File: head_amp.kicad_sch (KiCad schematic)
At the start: 50 parts, among them J1 USB Port, J2 I2C, J3 LED, J4 Left_Mic, J5 Left_Speaker, J6 Right_Mic, J7 Right_Speaker, J8 Fan, Q1 MMBT3904, Q2 MMBT3904, Q3 AO3401A, Q4 AO3400A, SW1 SW_Push, SW2 SW_Push, U1 AMS1117-3.3, U2 CH340K, U4 Headphone Jack, U7 AMS1117-3.3, U8 ESP32-WROOM-32E

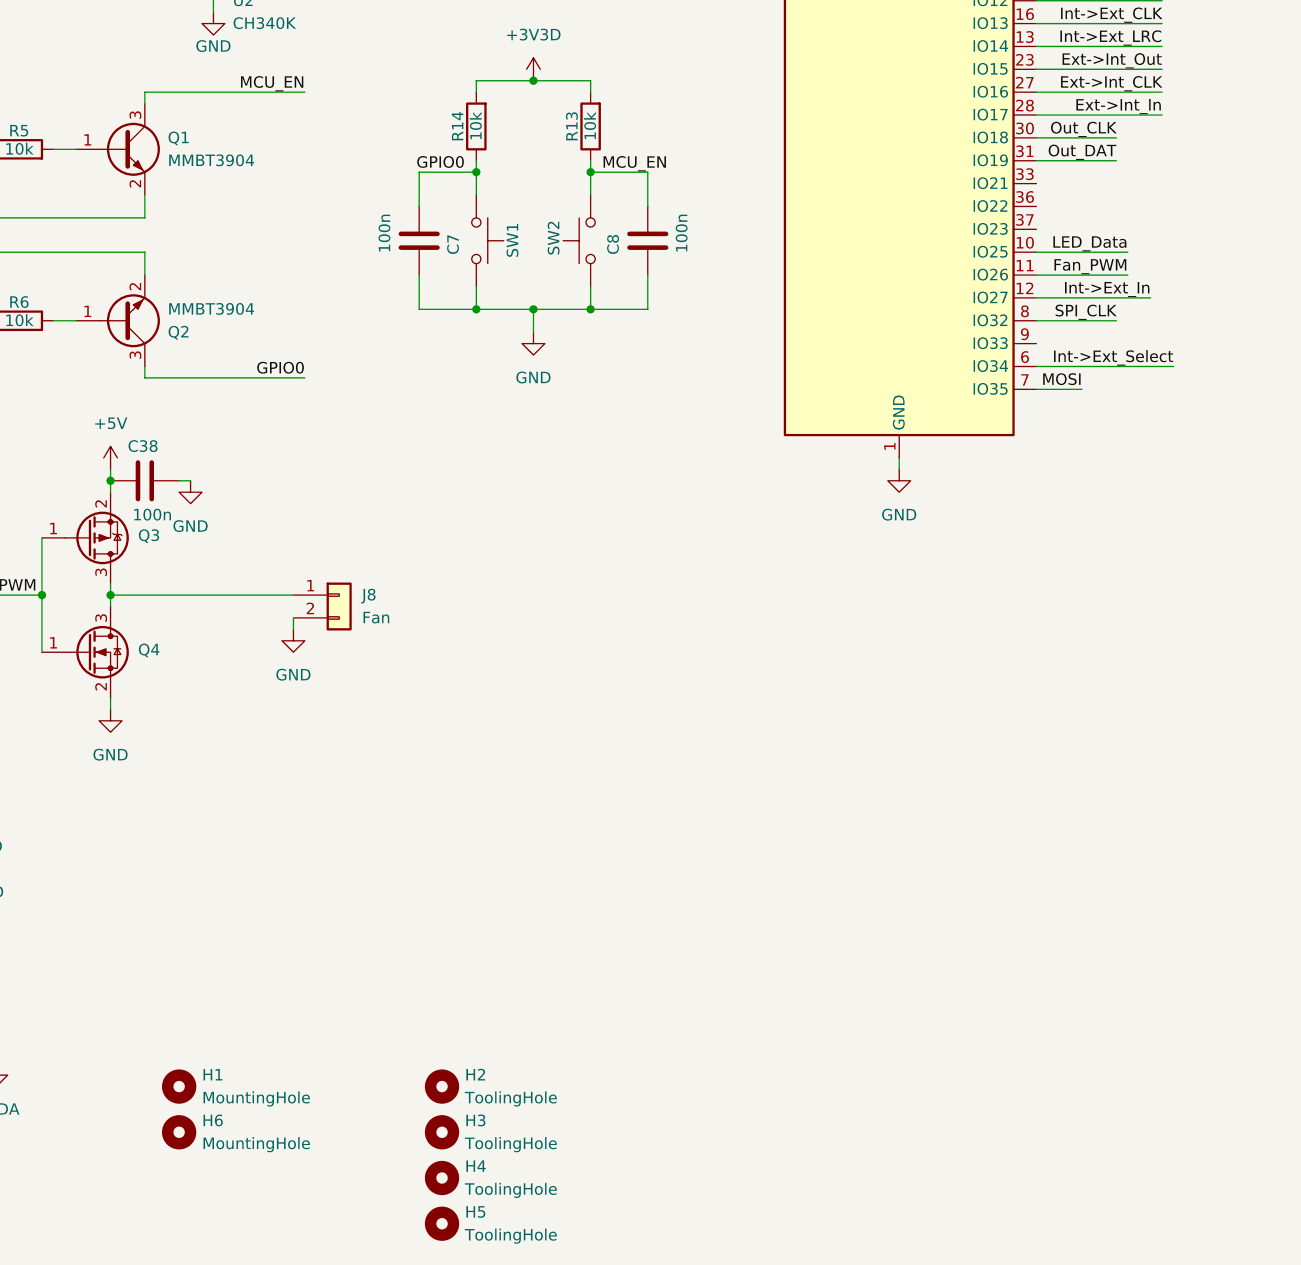
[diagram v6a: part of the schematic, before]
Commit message: Add holes and generic control button
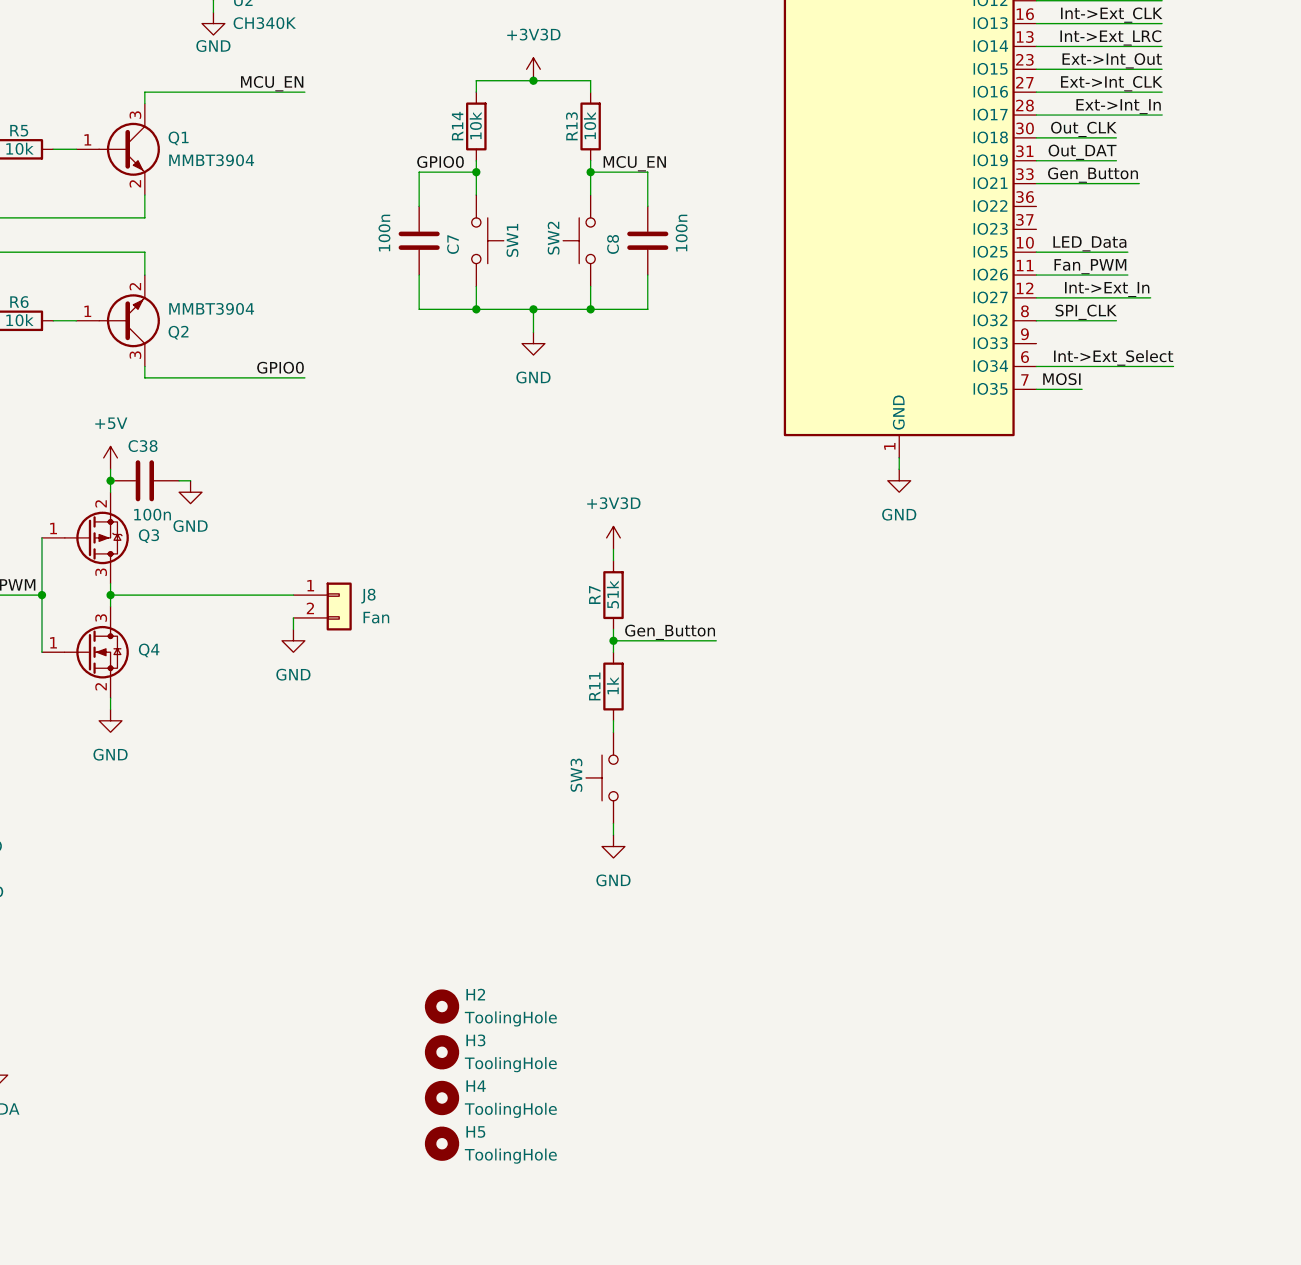
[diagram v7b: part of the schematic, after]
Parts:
- removed H1, H6: MountingHole, MountingHole:MountingHole_3.2mm_M3, symbol Mechanical:MountingHole
- added R11: 1k, Resistor_SMD:R_0402_1005Metric, symbol Device:R
- added R7: 51k, Resistor_SMD:R_0402_1005Metric, symbol Device:R
- added SW3: SW_Push, Button_Switch_SMD:SW_SPST_TS-1088-xR020, symbol Switch:SW_Push
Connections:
- net +3V3D: now also R7.2
- net GND: now also SW3.1
- net Gen_Button: now reaches U8.33 (IO21)
- net Gen_Button: now also R11.2, R7.1
- new net: R11.1, SW3.2
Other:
- moved on the sheet: H2, H3, H4, H5

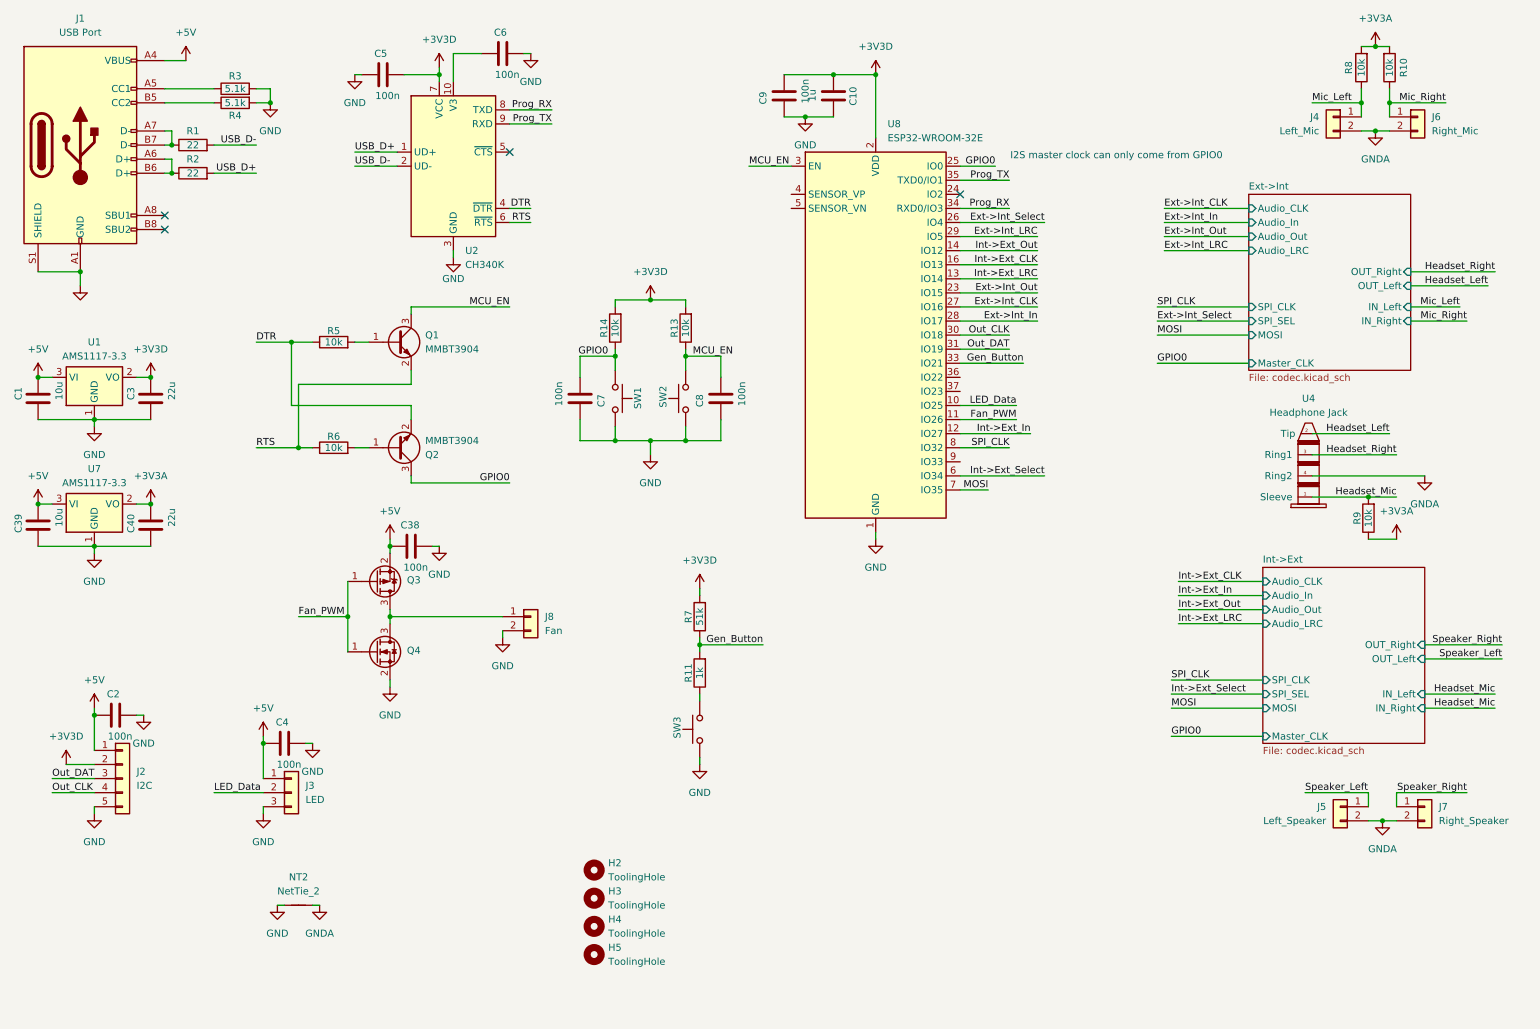
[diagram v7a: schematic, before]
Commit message: Add second expansion port
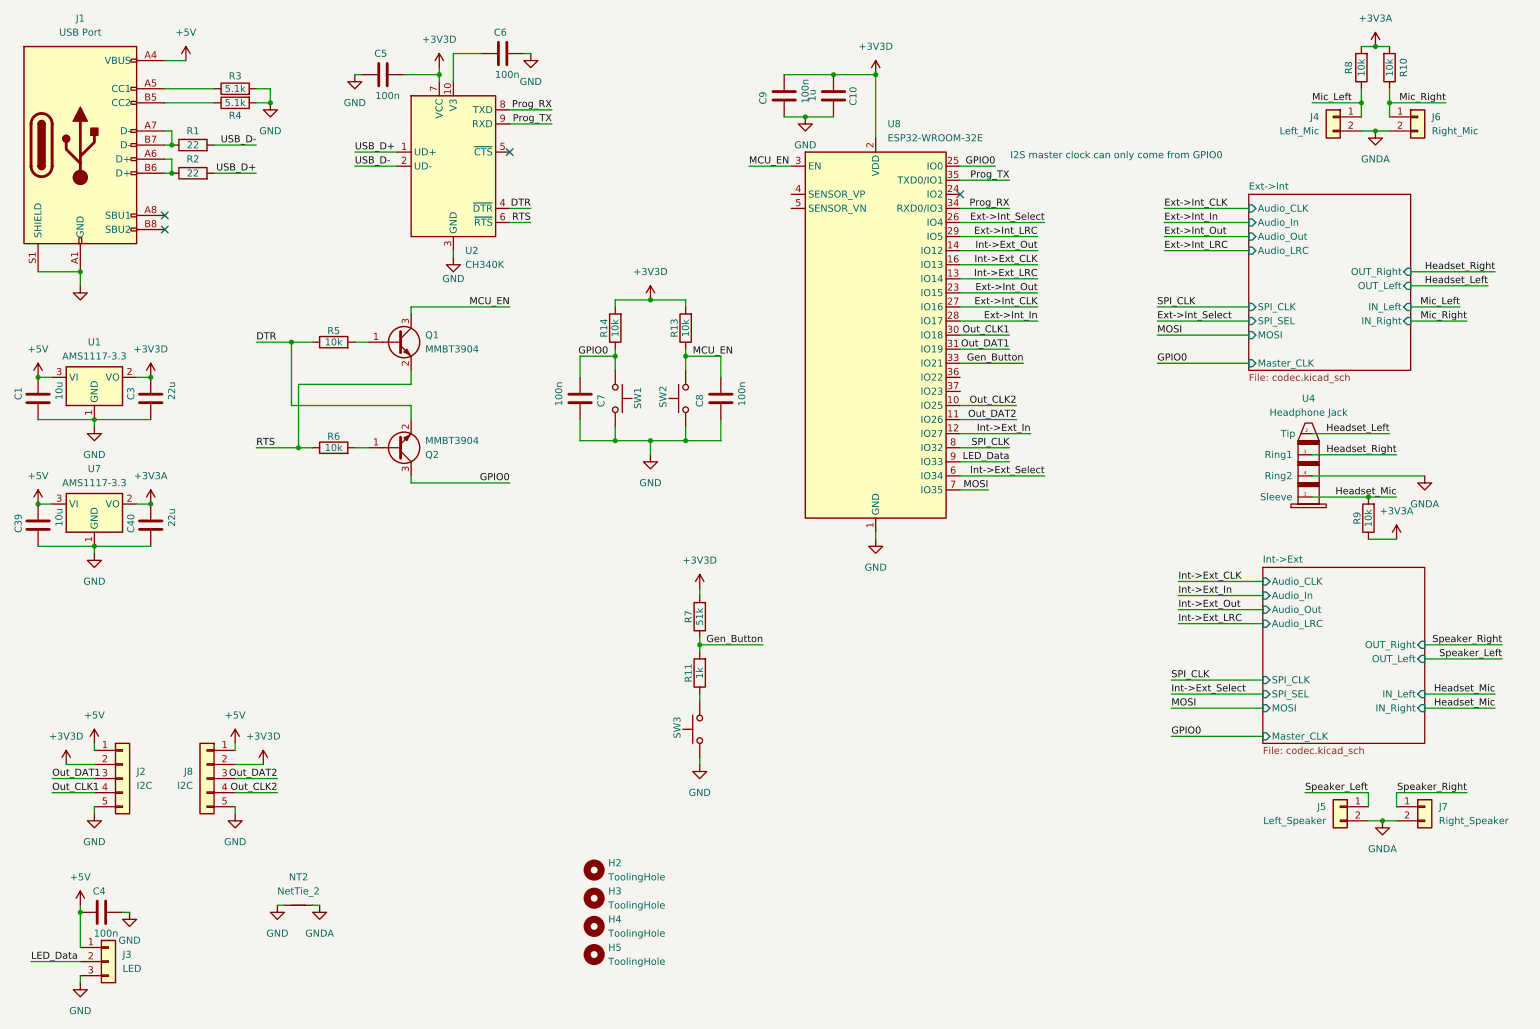
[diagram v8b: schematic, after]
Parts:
- removed C2, C38: 100n, Capacitor_SMD:C_0603_1608Metric, symbol Device:C
- removed J8: Fan, Connector_JST:JST_EH_S2B-EH_1x02_P2.50mm_Horizontal, symbol Connector_Generic:Conn_01x02
- removed Q3: AO3401A, Package_TO_SOT_SMD:SOT-23, symbol Transistor_FET:AO3401A
- removed Q4: AO3400A, Package_TO_SOT_SMD:SOT-23, symbol Transistor_FET:AO3400A
- added J8: I2C, Connector_JST:JST_EH_S5B-EH_1x05_P2.50mm_Horizontal, symbol Connector_Generic:Conn_01x05
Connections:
- net +3V3D: now also J8.2 (Pin_2)
- net +5V: now also J8.1 (Pin_1)
- net GND: now also J8.5 (Pin_5)
- net LED_Data: now also U8.9 (IO33); no longer U8.10 (IO25)
- net Fan_PWM renamed Out_DAT2
- net Out_DAT2: now also J8.3 (Pin_3)
- net Out_CLK renamed Out_CLK1
- net Out_DAT renamed Out_DAT1
- new net Out_CLK2: J8.4 (Pin_4), U8.10 (IO25)
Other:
- moved on the sheet: C4, J3
